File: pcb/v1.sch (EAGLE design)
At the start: 54 parts, among them U2 MMBT3904, U3 MMBT3904, U4 MMBT3904, U5 MMBT3904

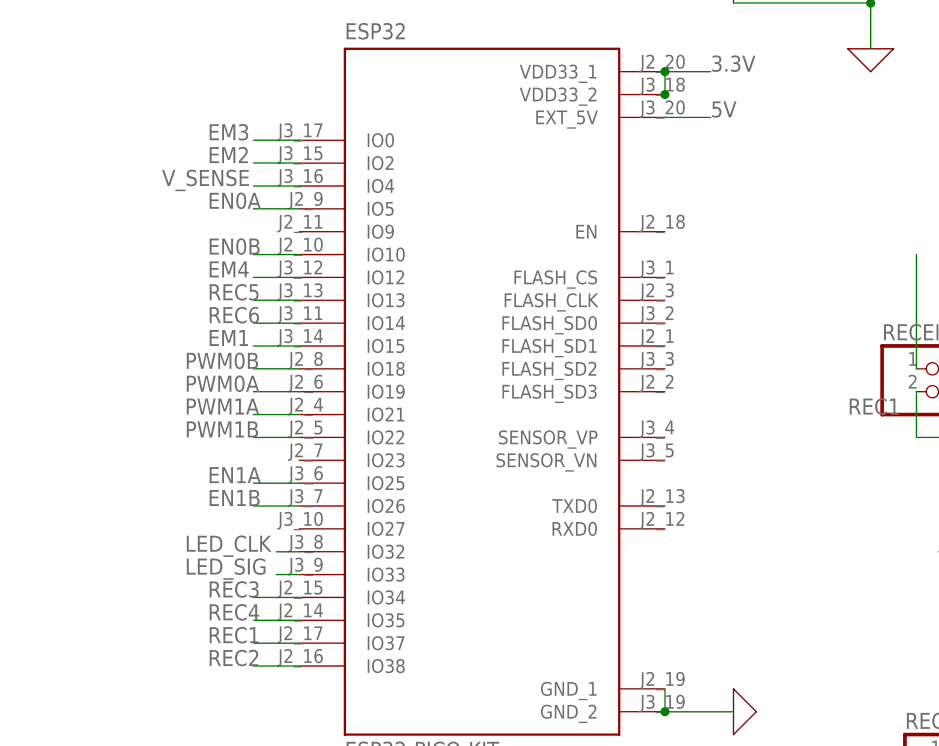
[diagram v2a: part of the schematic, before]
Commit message: Fixed led positioning and adc pins
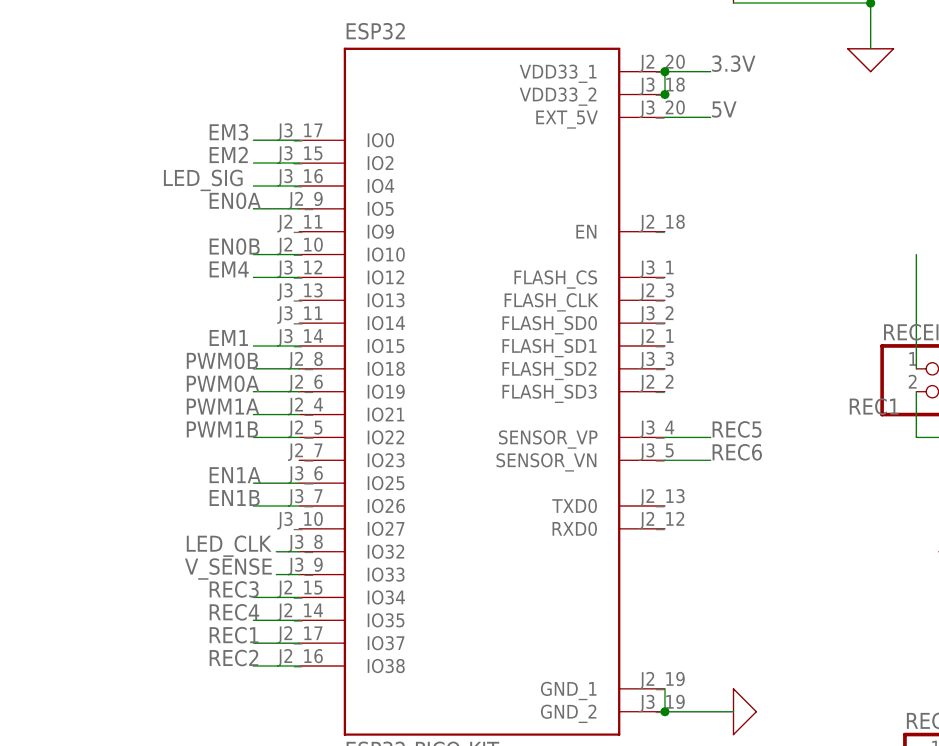
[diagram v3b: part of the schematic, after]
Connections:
- net LED_SIG: now also ESP32.IO4; no longer ESP32.IO33
- net REC5: now also ESP32.SENSOR_VP; no longer ESP32.IO13
- net REC6: now also ESP32.SENSOR_VN; no longer ESP32.IO14
- net V_SENSE: now also ESP32.IO33; no longer ESP32.IO4
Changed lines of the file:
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@@
 <net name="REC5" class="0">
-<segment>
-<pinref part="ESP32" gate="G$1" pin="IO13"/>
-<wire x1="63.5" y1="63.5" x2="58.42" y2="63.5" width="0.1524" layer="91"/>
-<label x="53.34" y="63.5" size="1.778" layer="95"/>
-</segment>
 <segment>
 <pinref part="RECEIVER5" gate="G$1" pin="2"/>
@@
 <wire x1="157.48" y1="5.08" x2="162.56" y2="5.08" width="0.1524" layer="91"/>
 </segment>
+<segment>
+<pinref part="ESP32" gate="G$1" pin="SENSOR_VP"/>
+<wire x1="104.14" y1="48.26" x2="109.22" y2="48.26" width="0.1524" layer="91"/>
+<label x="109.22" y="48.26" size="1.778" layer="95"/>
+</segment>
 </net>
 <net name="REC6" class="0">
-<segment>
-<pinref part="ESP32" gate="G$1" pin="IO14"/>
-<wire x1="63.5" y1="60.96" x2="58.42" y2="60.96" width="0.1524" layer="91"/>
-<label x="53.34" y="60.96" size="1.778" layer="95"/>
-</segment>
 <segment>
 <pinref part="RECEIVER6" gate="G$1" pin="2"/>
@@
 <wire x1="185.42" y1="5.08" x2="190.5" y2="5.08" width="0.1524" layer="91"/>
 </segment>
+<segment>
+<pinref part="ESP32" gate="G$1" pin="SENSOR_VN"/>
+<wire x1="104.14" y1="45.72" x2="109.22" y2="45.72" width="0.1524" layer="91"/>
+<label x="109.22" y="45.72" size="1.778" layer="95"/>
+</segment>
 </net>
 <net name="V_SENSE" class="0">
-<segment>
-<pinref part="ESP32" gate="G$1" pin="IO4"/>
-<wire x1="63.5" y1="76.2" x2="58.42" y2="76.2" width="0.1524" layer="91"/>
-<label x="48.26" y="76.2" size="1.778" layer="95"/>
-</segment>
 <segment>
 <pinref part="R19" gate="G$1" pin="2"/>
@@
 <label x="-20.32" y="134.62" size="1.778" layer="95"/>
 <junction x="-20.32" y="127"/>
+</segment>
+<segment>
+<pinref part="ESP32" gate="G$1" pin="IO33"/>
+<wire x1="63.5" y1="33.02" x2="60.96" y2="33.02" width="0.1524" layer="91"/>
+<label x="50.8" y="33.02" size="1.778" layer="95"/>
 </segment>
 </net>
@@
 <net name="LED_SIG" class="0">
 <segment>
-<pinref part="ESP32" gate="G$1" pin="IO33"/>
-<wire x1="63.5" y1="33.02" x2="60.96" y2="33.02" width="0.1524" layer="91"/>
-<label x="50.8" y="33.02" size="1.778" layer="95"/>
-</segment>
-<segment>
 <pinref part="D1" gate="G$1" pin="DI"/>
 <wire x1="144.78" y1="124.46" x2="142.24" y2="124.46" width="0.1524" layer="91"/>
 <label x="132.08" y="124.46" size="1.778" layer="95"/>
 </segment>
-</net>
+<segment>
+<pinref part="ESP32" gate="G$1" pin="IO4"/>
+<wire x1="63.5" y1="76.2" x2="58.42" y2="76.2" width="0.1524" layer="91"/>
+<label x="48.26" y="76.2" size="1.778" layer="95"/>
+</segment>
+</net>

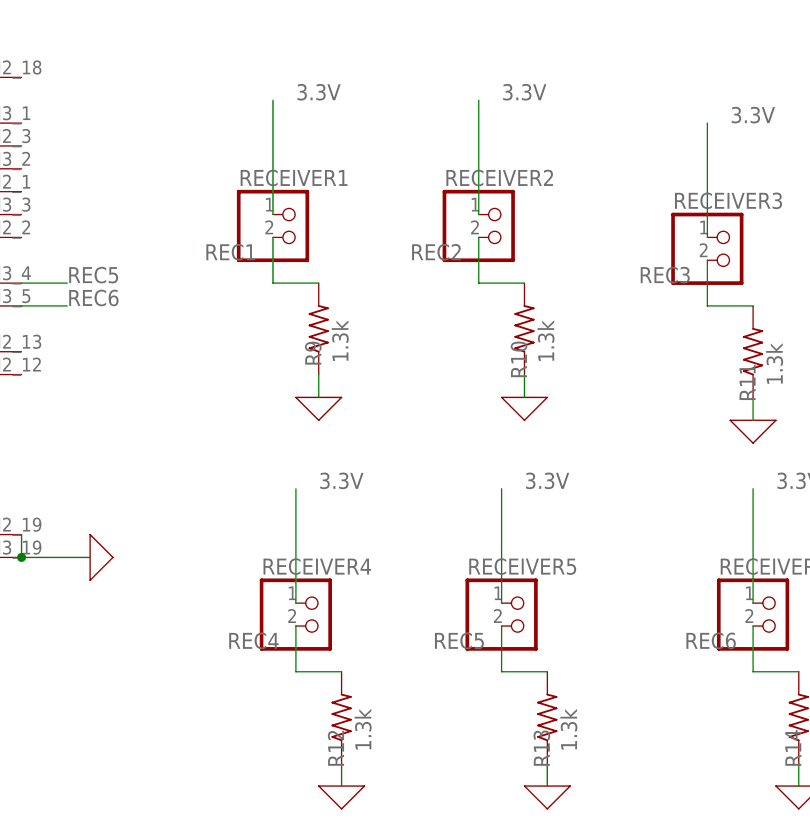
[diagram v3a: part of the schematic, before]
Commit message: Changed pin placement
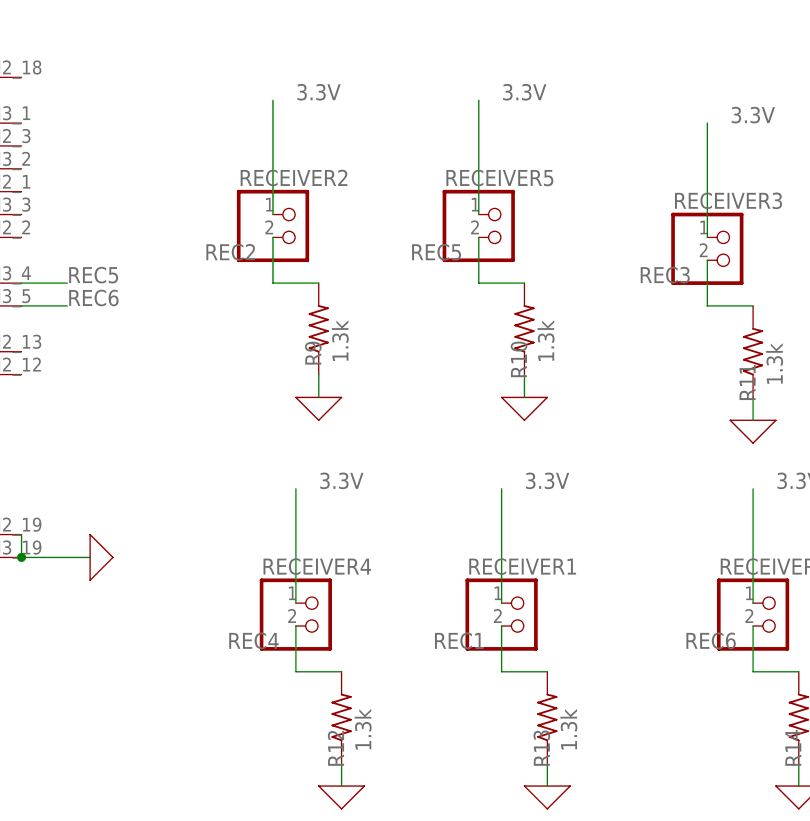
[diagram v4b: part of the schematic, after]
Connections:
- net REC1: now also R13.2; no longer R9.2
- net REC2: now also R9.2; no longer R10.2
- net REC5: now also R10.2; no longer R13.2
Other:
- moved on the sheet: RECEIVER1, RECEIVER2, RECEIVER5
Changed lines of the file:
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@@
 <part name="U2" library="transistors" deviceset="MMBT3904" device=""/>
 <part name="R2" library="rcl" library_urn="urn:adsk.eagle:library:334" deviceset="R-US_" device="M1206" package3d_urn="urn:adsk.eagle:package:23566/1" value="100"/>
-<part name="RECEIVER1" library="pinhead" library_urn="urn:adsk.eagle:library:325" deviceset="PINHD-1X2" device="" package3d_urn="urn:adsk.eagle:package:22435/2"/>
+<part name="RECEIVER2" library="pinhead" library_urn="urn:adsk.eagle:library:325" deviceset="PINHD-1X2" device="" package3d_urn="urn:adsk.eagle:package:22435/2"/>
 <part name="R9" library="rcl" library_urn="urn:adsk.eagle:library:334" deviceset="R-US_" device="M1206" package3d_urn="urn:adsk.eagle:package:23566/1" value="1.3k"/>
 <part name="X_7" library="ngspice-simulation" library_urn="urn:adsk.eagle:library:527439" deviceset="GND" device=""/>
-<part name="RECEIVER2" library="pinhead" library_urn="urn:adsk.eagle:library:325" deviceset="PINHD-1X2" device="" package3d_urn="urn:adsk.eagle:package:22435/2"/>
+<part name="RECEIVER5" library="pinhead" library_urn="urn:adsk.eagle:library:325" deviceset="PINHD-1X2" device="" package3d_urn="urn:adsk.eagle:package:22435/2"/>
 <part name="R10" library="rcl" library_urn="urn:adsk.eagle:library:334" deviceset="R-US_" device="M1206" package3d_urn="urn:adsk.eagle:package:23566/1" value="1.3k"/>
 <part name="X_8" library="ngspice-simulation" library_urn="urn:adsk.eagle:library:527439" deviceset="GND" device=""/>
@@
 <part name="R12" library="rcl" library_urn="urn:adsk.eagle:library:334" deviceset="R-US_" device="M1206" package3d_urn="urn:adsk.eagle:package:23566/1" value="1.3k"/>
 <part name="X_10" library="ngspice-simulation" library_urn="urn:adsk.eagle:library:527439" deviceset="GND" device=""/>
-<part name="RECEIVER5" library="pinhead" library_urn="urn:adsk.eagle:library:325" deviceset="PINHD-1X2" device="" package3d_urn="urn:adsk.eagle:package:22435/2"/>
+<part name="RECEIVER1" library="pinhead" library_urn="urn:adsk.eagle:library:325" deviceset="PINHD-1X2" device="" package3d_urn="urn:adsk.eagle:package:22435/2"/>
 <part name="R13" library="rcl" library_urn="urn:adsk.eagle:library:334" deviceset="R-US_" device="M1206" package3d_urn="urn:adsk.eagle:package:23566/1" value="1.3k"/>
 <part name="X_11" library="ngspice-simulation" library_urn="urn:adsk.eagle:library:527439" deviceset="GND" device=""/>
@@
 <attribute name="VALUE" x="-11.43" y="74.422" size="1.778" layer="96" rot="R180"/>
 </instance>
-<instance part="RECEIVER1" gate="G$1" x="134.62" y="53.34" smashed="yes">
+<instance part="RECEIVER2" gate="G$1" x="134.62" y="53.34" smashed="yes">
 <attribute name="NAME" x="128.27" y="59.055" size="1.778" layer="95"/>
 <attribute name="VALUE" x="128.27" y="48.26" size="1.778" layer="96"/>
@@
 </instance>
 <instance part="X_7" gate="G$1" x="137.16" y="35.56" smashed="yes"/>
-<instance part="RECEIVER2" gate="G$1" x="157.48" y="53.34" smashed="yes">
+<instance part="RECEIVER5" gate="G$1" x="157.48" y="53.34" smashed="yes">
 <attribute name="NAME" x="151.13" y="59.055" size="1.778" layer="95"/>
 <attribute name="VALUE" x="151.13" y="48.26" size="1.778" layer="96"/>
@@
 </instance>
 <instance part="X_10" gate="G$1" x="139.7" y="-7.62" smashed="yes"/>
-<instance part="RECEIVER5" gate="G$1" x="160.02" y="10.16" smashed="yes">
+<instance part="RECEIVER1" gate="G$1" x="160.02" y="10.16" smashed="yes">
 <attribute name="NAME" x="153.67" y="15.875" size="1.778" layer="95"/>
 <attribute name="VALUE" x="153.67" y="5.08" size="1.778" layer="96"/>
@@
 </segment>
 <segment>
-<pinref part="RECEIVER1" gate="G$1" pin="1"/>
+<pinref part="RECEIVER2" gate="G$1" pin="1"/>
 <label x="134.62" y="68.58" size="1.778" layer="95"/>
 <wire x1="132.08" y1="55.88" x2="132.08" y2="68.58" width="0.1524" layer="91"/>
 </segment>
 <segment>
-<pinref part="RECEIVER2" gate="G$1" pin="1"/>
+<pinref part="RECEIVER5" gate="G$1" pin="1"/>
 <label x="157.48" y="68.58" size="1.778" layer="95"/>
 <wire x1="154.94" y1="55.88" x2="154.94" y2="68.58" width="0.1524" layer="91"/>
@@
 </segment>
 <segment>
-<pinref part="RECEIVER5" gate="G$1" pin="1"/>
+<pinref part="RECEIVER1" gate="G$1" pin="1"/>
 <label x="160.02" y="25.4" size="1.778" layer="95"/>
 <wire x1="157.48" y1="12.7" x2="157.48" y2="25.4" width="0.1524" layer="91"/>
@@
 <segment>
 <pinref part="RECEIVER1" gate="G$1" pin="2"/>
+<label x="149.86" y="7.62" size="1.778" layer="95"/>
+<pinref part="R13" gate="G$1" pin="2"/>
+<wire x1="157.48" y1="10.16" x2="157.48" y2="5.08" width="0.1524" layer="91"/>
+<wire x1="157.48" y1="5.08" x2="162.56" y2="5.08" width="0.1524" layer="91"/>
+</segment>
+</net>
+<net name="REC2" class="0">
+<segment>
+<pinref part="ESP32" gate="G$1" pin="IO38"/>
+<wire x1="63.5" y1="22.86" x2="58.42" y2="22.86" width="0.1524" layer="91"/>
+<label x="53.34" y="22.86" size="1.778" layer="95"/>
+</segment>
+<segment>
+<pinref part="RECEIVER2" gate="G$1" pin="2"/>
 <label x="124.46" y="50.8" size="1.778" layer="95"/>
 <pinref part="R9" gate="G$1" pin="2"/>
 <wire x1="132.08" y1="53.34" x2="132.08" y2="48.26" width="0.1524" layer="91"/>
 <wire x1="132.08" y1="48.26" x2="137.16" y2="48.26" width="0.1524" layer="91"/>
-</segment>
-</net>
-<net name="REC2" class="0">
-<segment>
-<pinref part="ESP32" gate="G$1" pin="IO38"/>
-<wire x1="63.5" y1="22.86" x2="58.42" y2="22.86" width="0.1524" layer="91"/>
-<label x="53.34" y="22.86" size="1.778" layer="95"/>
-</segment>
-<segment>
-<pinref part="RECEIVER2" gate="G$1" pin="2"/>
-<label x="147.32" y="50.8" size="1.778" layer="95"/>
-<pinref part="R10" gate="G$1" pin="2"/>
-<wire x1="154.94" y1="53.34" x2="154.94" y2="48.26" width="0.1524" layer="91"/>
-<wire x1="154.94" y1="48.26" x2="160.02" y2="48.26" width="0.1524" layer="91"/>
 </segment>
 </net>
@@
 <net name="REC5" class="0">
 <segment>
-<pinref part="RECEIVER5" gate="G$1" pin="2"/>
-<label x="149.86" y="7.62" size="1.778" layer="95"/>
-<pinref part="R13" gate="G$1" pin="2"/>
-<wire x1="157.48" y1="10.16" x2="157.48" y2="5.08" width="0.1524" layer="91"/>
-<wire x1="157.48" y1="5.08" x2="162.56" y2="5.08" width="0.1524" layer="91"/>
-</segment>
-<segment>
 <pinref part="ESP32" gate="G$1" pin="SENSOR_VP"/>
 <wire x1="104.14" y1="48.26" x2="109.22" y2="48.26" width="0.1524" layer="91"/>
 <label x="109.22" y="48.26" size="1.778" layer="95"/>
 </segment>
+<segment>
+<pinref part="RECEIVER5" gate="G$1" pin="2"/>
+<label x="147.32" y="50.8" size="1.778" layer="95"/>
+<pinref part="R10" gate="G$1" pin="2"/>
+<wire x1="154.94" y1="53.34" x2="154.94" y2="48.26" width="0.1524" layer="91"/>
+<wire x1="154.94" y1="48.26" x2="160.02" y2="48.26" width="0.1524" layer="91"/>
+</segment>
 </net>
 <net name="REC6" class="0">
+<segment>
+<pinref part="ESP32" gate="G$1" pin="SENSOR_VN"/>
+<wire x1="104.14" y1="45.72" x2="109.22" y2="45.72" width="0.1524" layer="91"/>
+<label x="109.22" y="45.72" size="1.778" layer="95"/>
+</segment>
 <segment>
 <pinref part="RECEIVER6" gate="G$1" pin="2"/>
@@
 <wire x1="185.42" y1="5.08" x2="190.5" y2="5.08" width="0.1524" layer="91"/>
 </segment>
-<segment>
-<pinref part="ESP32" gate="G$1" pin="SENSOR_VN"/>
-<wire x1="104.14" y1="45.72" x2="109.22" y2="45.72" width="0.1524" layer="91"/>
-<label x="109.22" y="45.72" size="1.778" layer="95"/>
-</segment>
-</net>
+</net>
